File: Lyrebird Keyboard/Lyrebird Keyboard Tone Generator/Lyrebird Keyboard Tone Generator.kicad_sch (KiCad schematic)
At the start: 111 parts, among them IC1 LM358DT, IC10 LM358DT, IC11 LM358DT, IC12 LM358DT, IC13 HEF4069UBT,653, IC14 HEF4069UBT,653, IC2 LM358DT, IC3 LM358DT, IC4 LM358DT, IC5 LM358DT, IC6 LM358DT, IC7 LM358DT, IC8 LM358DT, IC9 LM358DT, J1 Edge Connector, J10 C# 4434 Hz, J11 G# 6642 Hz, J12 D 4697 Hz, J13 F# 5923 Hz, J2 A 3520 Hz, J3 D# 4976 Hz, J4 A# 3726 Hz, J5 E 5274 Hz, J6 B 3949 Hz, J7 F 5590 Hz, J8 C 4188 Hz, J9 G 6275 Hz

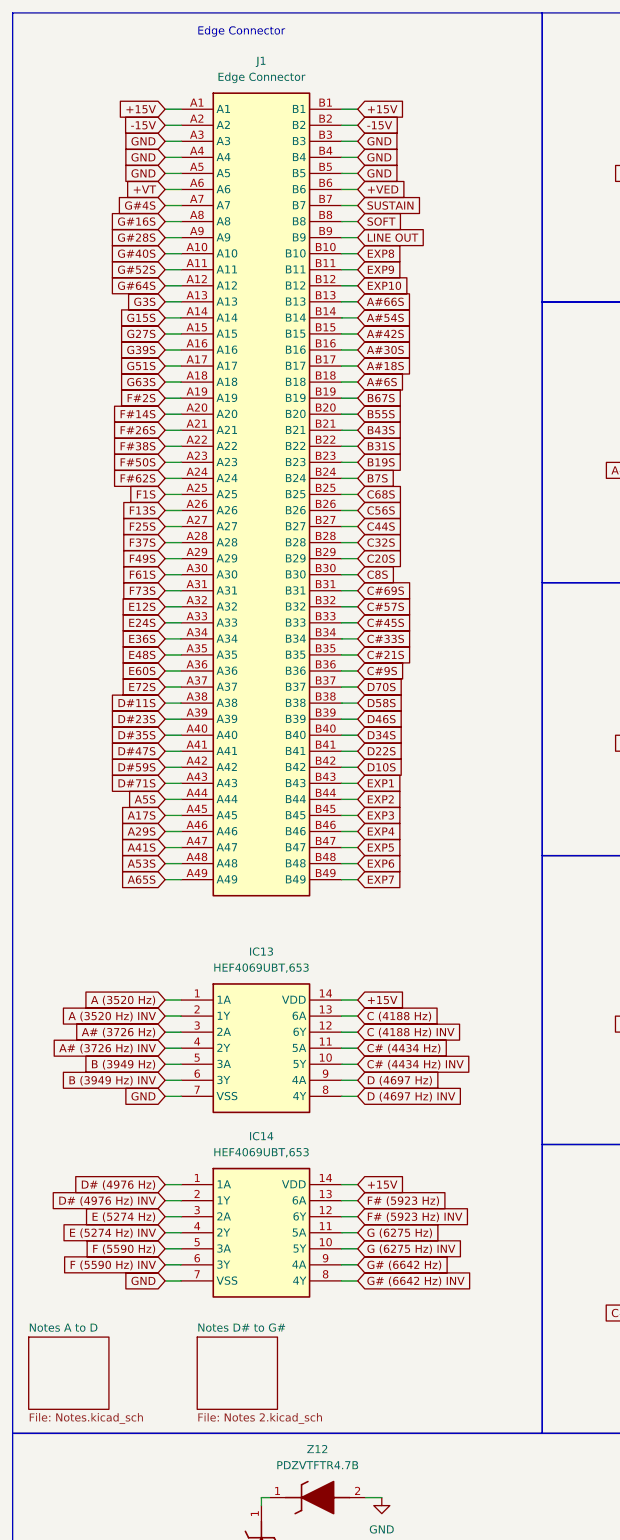
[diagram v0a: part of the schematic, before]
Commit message: Major Design Changes
Completed Tone Generator Board, board now only provides base notes, individual notes will be generated on the wave shaping boards.

Made major changes to pci slot config, and have increased grounding of the slots.

May need decoupling capacitors on tone generator board, but tight for room
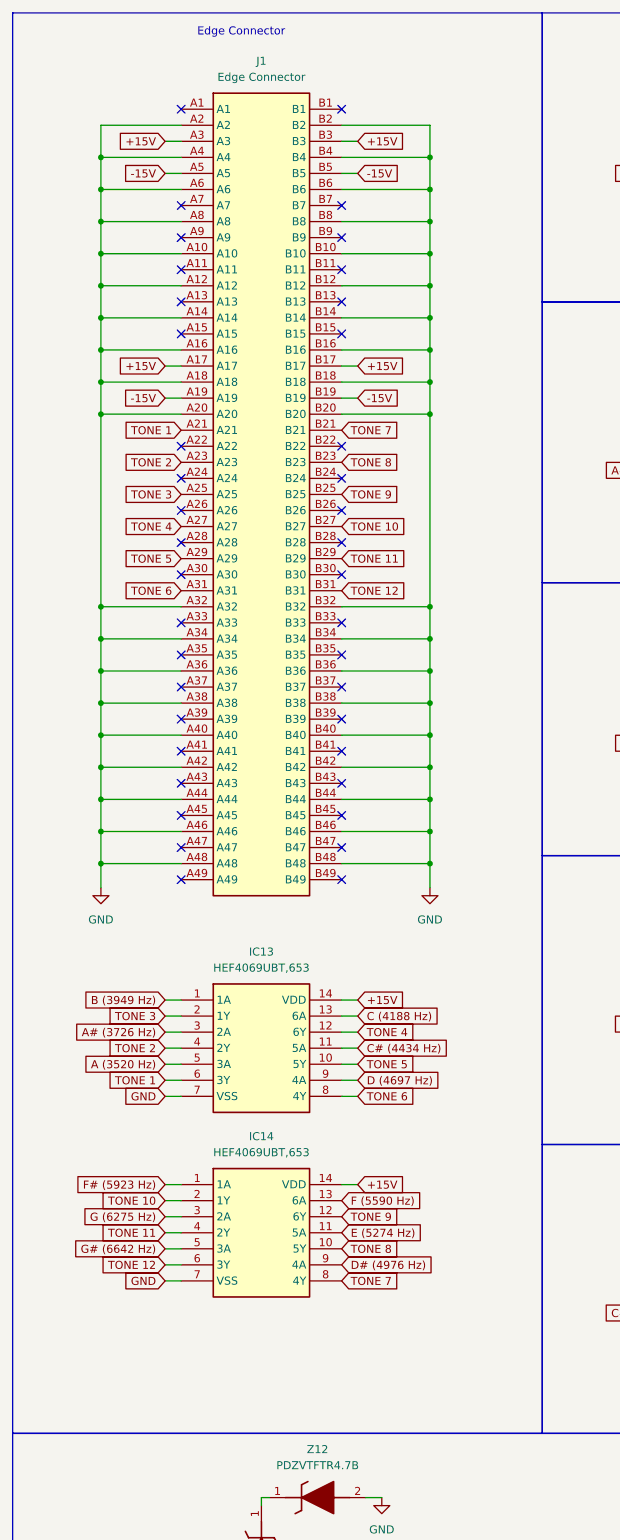
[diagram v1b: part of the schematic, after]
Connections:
- net +VED is gone; now on net GND: J1.B6
- net +VT is gone; now on net GND: J1.A6
- net A#18S is gone; now on net +15V: J1.B17
- net A#30S is gone; now on net GND: J1.B16
- net A#54S is gone; now on net GND: J1.B14
- net A#6S is gone; now on net GND: J1.B18
- net A29S is gone; now on net GND: J1.A46
- net A53S is gone; now on net GND: J1.A48
- net A5S is gone; now on net GND: J1.A44
- net B55S is gone; now on net GND: J1.B20
- net B67S is gone; now on net -15V: J1.B19
- net C#33S is gone; now on net GND: J1.B34
- net C#57S is gone; now on net GND: J1.B32
- net C#9S is gone; now on net GND: J1.B36
- net D# (4976 Hz) INV is gone; now on net TONE 10: IC14.2 (1Y)
- net D#11S is gone; now on net GND: J1.A38
- net D#35S is gone; now on net GND: J1.A40
- net D#59S is gone; now on net GND: J1.A42
- net D10S is gone; now on net GND: J1.B42
- net D34S is gone; now on net GND: J1.B40
- net D58S is gone; now on net GND: J1.B38
- net E (5274 Hz) INV is gone; now on net TONE 11: IC14.4 (2Y)
- net E12S is gone; now on net GND: J1.A32
- net E36S is gone; now on net GND: J1.A34
- net E60S is gone; now on net GND: J1.A36
- net EXP10 is gone; now on net GND: J1.B12
- net EXP2 is gone; now on net GND: J1.B44
- net EXP4 is gone; now on net GND: J1.B46
- net EXP6 is gone; now on net GND: J1.B48
- net EXP8 is gone; now on net GND: J1.B10
- net F (5590 Hz) INV is gone; now on net TONE 12: IC14.6 (3Y)
- net F# (5923 Hz) INV is gone; now on net TONE 9: IC14.12 (6Y)
- net F#14S is gone; now on net GND: J1.A20
- net F#26S is gone; now on net TONE 1: J1.A21
- net F#2S is gone; now on net -15V: J1.A19
- net F#50S is gone; now on net TONE 2: J1.A23
- net F1S is gone; now on net TONE 3: J1.A25
- net F25S is gone; now on net TONE 4: J1.A27
- net F49S is gone; now on net TONE 5: J1.A29
- net F73S is gone; now on net TONE 6: J1.A31
- net G (6275 Hz) INV is gone; now on net TONE 8: IC14.10 (5Y)
- net G# (6642 Hz) INV is gone; now on net TONE 7: IC14.8 (4Y)
- net G#16S is gone; now on net GND: J1.A8
- net G#40S is gone; now on net GND: J1.A10
- net G#64S is gone; now on net GND: J1.A12
- net G15S is gone; now on net GND: J1.A14
- net G39S is gone; now on net GND: J1.A16
- net G51S is gone; now on net +15V: J1.A17
- net G63S is gone; now on net GND: J1.A18
- net SOFT is gone; now on net GND: J1.B8
- net +15V: now also J1.A3, J1.B3; no longer J1.A1, J1.B1
- net -15V: now also J1.A5, J1.B5; no longer J1.A2, J1.B2
- net A (3520 Hz): now also IC13.5 (3A); no longer IC13.1 (1A)
- net B (3949 Hz): now also IC13.1 (1A); no longer IC13.5 (3A)
- net D# (4976 Hz): now also IC14.9 (4A); no longer IC14.1 (1A)
- net E (5274 Hz): now also IC14.11 (5A); no longer IC14.3 (2A)
- net F (5590 Hz): now also IC14.13 (6A); no longer IC14.5 (3A)
- net F# (5923 Hz): now also IC14.1 (1A); no longer IC14.13 (6A)
- net G (6275 Hz): now also IC14.3 (2A); no longer IC14.11 (5A)
- net G# (6642 Hz): now also IC14.5 (3A); no longer IC14.9 (4A)
- net GND: now also J1.A2, J1.B2; no longer J1.A3, J1.A5, J1.B3, J1.B5
- net A (3520 Hz) INV renamed TONE 3
- net A# (3726 Hz) INV renamed TONE 2
- net A#42S: no longer names the net of J1.B15
- net A#66S: no longer names the net of J1.B13
- net A17S: no longer names the net of J1.A45
- net A41S: no longer names the net of J1.A47
- net A65S: no longer names the net of J1.A49
- net B (3949 Hz) INV renamed TONE 1
- net B19S renamed TONE 8
- net B31S: no longer names the net of J1.B22
- net B43S renamed TONE 7
- net B7S: no longer names the net of J1.B24
- net C (4188 Hz) INV renamed TONE 4
- net C# (4434 Hz) INV renamed TONE 5
- net C#21S: no longer names the net of J1.B35
- net C#45S: no longer names the net of J1.B33
- net C#69S renamed TONE 12
- net C20S renamed TONE 11
- net C32S: no longer names the net of J1.B28
- net C44S renamed TONE 10
- net C56S: no longer names the net of J1.B26
- net C68S renamed TONE 9
- net C8S: no longer names the net of J1.B30
- net D (4697 Hz) INV renamed TONE 6
- net D#23S: no longer names the net of J1.A39
- net D#47S: no longer names the net of J1.A41
- net D#71S: no longer names the net of J1.A43
- net D22S: no longer names the net of J1.B41
- net D46S: no longer names the net of J1.B39
- net D70S: no longer names the net of J1.B37
- net E24S: no longer names the net of J1.A33
- net E48S: no longer names the net of J1.A35
- net E72S: no longer names the net of J1.A37
- net EXP1: no longer names the net of J1.B43
- net EXP3: no longer names the net of J1.B45
- net EXP5: no longer names the net of J1.B47
- net EXP7: no longer names the net of J1.B49
- net EXP9: no longer names the net of J1.B11
- net F#38S: no longer names the net of J1.A22
- net F#62S: no longer names the net of J1.A24
- net F13S: no longer names the net of J1.A26
- net F37S: no longer names the net of J1.A28
- net F61S: no longer names the net of J1.A30
- net G#28S: no longer names the net of J1.A9
- net G#4S: no longer names the net of J1.A7
- net G#52S: no longer names the net of J1.A11
- net G27S: no longer names the net of J1.A15
- net G3S: no longer names the net of J1.A13
- net LINE OUT: no longer names the net of J1.B9
- net SUSTAIN: no longer names the net of J1.B7
- no-connect marks 12 -> 52
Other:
- removed sheet Notes A to D
- removed sheet Notes D# to G#

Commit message: Schematic Updates
Made updates to schematics, to use correct symbols, and minor PCB updates, further work on the piano card design
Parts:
- removed IC1, IC10, IC11, IC12, IC2, IC3, IC4, IC5, IC6, IC7, IC8, IC9: LM358DT, SamacSys_Parts:SOIC127P600X175-8N, symbol SamacSys_Parts:LM358DT
- removed IC13, IC14: HEF4069UBT,653, SOIC127P600X175-14N, symbol SamacSys_Parts:HEF4069UBT,653
- added U1, U10, U11, U12, U2, U3, U4, U5, U6, U7, U8, U9: LM358, SamacSys_Parts:SOIC127P600X175-8N, symbol Amplifier_Operational:LM358
- added U13, U14: 4069, SamacSys_Parts:SOIC127P600X175-14N, symbol 4xxx:4069
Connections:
- net +15V: now also U1.8 (V+), U10.8 (V+), U11.8 (V+), U12.8 (V+), U13.14 (VDD), U14.14 (VDD), U2.8 (V+), U3.8 (V+), U4.8 (V+), U5.8 (V+), U6.8 (V+), U7.8 (V+), U8.8 (V+), U9.8 (V+)
- net -15V: now also U1.4 (V-), U10.4 (V-), U11.4 (V-), U12.4 (V-), U2.4 (V-), U3.4 (V-), U4.4 (V-), U5.4 (V-), U6.4 (V-), U7.4 (V-), U8.4 (V-), U9.4 (V-)
- net A (3520 Hz): now also R2.2, R3.2, U13.5; no longer R1.2, R3.1
- net A# (3726 Hz): now also R6.2, R7.2, U13.3; no longer R5.2, R7.1
- net B (3949 Hz): now also R10.2, R11.2, U13.1; no longer R11.1, R9.2
- net C (4188 Hz): now also R14.2, R15.2, R16.3, U13.13; no longer R13.2, R15.1, R16.1 (CCW)
- net C# (4434 Hz): now also R18.2, R19.2, R20.3, U13.11; no longer R17.2, R19.1, R20.1 (CCW)
- net D (4697 Hz): now also R22.2, R23.2, R24.3, U13.9; no longer R21.2, R23.1, R24.1 (CCW)
- net D# (4976 Hz): now also R26.2, R37.2, R43.3, U14.9; no longer R25.2, R37.1, R43.1 (CCW)
- net E (5274 Hz): now also R28.2, R38.2, R44.3, U14.11; no longer R27.2, R38.1, R44.1 (CCW)
- net F (5590 Hz): now also R30.2, R39.2, R45.3, U14.13; no longer R29.2, R39.1, R45.1 (CCW)
- net F# (5923 Hz): now also R36.2, R42.2, R48.3, U14.1; no longer R35.2, R42.1, R48.1 (CCW)
- net G (6275 Hz): now also R32.2, R40.2, R46.3, U14.3; no longer R31.2, R40.1, R46.1 (CCW)
- net G# (6642 Hz): now also R34.2, R41.2, R47.3, U14.5; no longer R33.2, R41.1, R47.1 (CCW)
- net GND: now also U1.2 (-), U1.5 (+), U10.2 (-), U10.5 (+), U11.2 (-), U11.5 (+), U12.2 (-), U12.5 (+), U13.7 (VSS), U14.7 (VSS), U2.2 (-), U2.5 (+), U3.2 (-), U3.5 (+), U4.2 (-), U4.5 (+), U5.2 (-), U5.5 (+), U6.2 (-), U6.5 (+), U7.2 (-), U7.5 (+), U8.2 (-), U8.5 (+), U9.2 (-), U9.5 (+)
- net TONE 1: now also U13.6
- net TONE 10: now also U14.2
- net TONE 11: now also U14.4
- net TONE 12: now also U14.6
- net TONE 2: now also U13.4
- net TONE 3: now also U13.2
- net TONE 4: now also U13.12
- net TONE 5: now also U13.10
- net TONE 6: now also U13.8
- net TONE 7: now also U14.8
- net TONE 8: now also U14.10
- net TONE 9: now also U14.12
- net at C5.1, R20.2: now also U5.6 (-)
- net at R31.1: now also C10.2, U11.7; no longer R32.2
- net at C10.1, R46.2: now also U11.6 (-)
- net at C12.1, R48.2: now also U10.6 (-)
- net at C1.1, R4.2: now also U1.6 (-)
- net at R29.1: now also C9.2, U9.7; no longer R30.2
- net at C8.1, R44.2: now also U8.6 (-)
- net at C9.1, R45.2: now also U9.6 (-)
- net at C7.1, R43.2: now also U7.6 (-)
- net at R1.1: now also C1.2, U1.7; no longer R2.2
- net at R13.1: now also C4.2, U4.7; no longer R14.2
- net at C2.1, R8.2: now also U2.6 (-)
- net at C6.1, R24.2: now also U6.6 (-)
- net at C3.1, R12.2: now also U3.6 (-)
- net at R5.1: now also C2.2, U2.7; no longer R6.2
- net at C4.1, R16.2: now also U4.6 (-)
- net at R17.1: now also C5.2, U5.7; no longer R18.2
- net at R33.1: now also C11.2, U12.7; no longer R34.2
- net at C11.1, R47.2: now also U12.6 (-)
- net at R9.1: now also C3.2, U3.7; no longer R10.2
- net at R27.1: now also C8.2, U8.7; no longer R28.2
- net at R21.1: now also C6.2, U6.7; no longer R22.2
- net at R25.1: now also C7.2, U7.7; no longer R26.2
- net at R35.1: now also C12.2, U10.7; no longer R36.2
- net TRI WAVE OUT (A#): no longer names the net of R6.1
- net TRI WAVE OUT (A#): now also R5.2, U2.3 (+); no longer C2.2
- net TRI WAVE OUT (A): no longer names the net of R2.1
- net TRI WAVE OUT (A): now also R1.2, U1.3 (+); no longer C1.2
- net TRI WAVE OUT (B): no longer names the net of R10.1
- net TRI WAVE OUT (B): now also R9.2, U3.3 (+); no longer C3.2
- net TRI WAVE OUT (C#): no longer names the net of R18.1
- net TRI WAVE OUT (C#): now also R17.2, U5.3 (+); no longer C5.2
- net TRI WAVE OUT (C): no longer names the net of R14.1
- net TRI WAVE OUT (C): now also R13.2, U4.3 (+); no longer C4.2
- net TRI WAVE OUT (D#): no longer names the net of R26.1
- net TRI WAVE OUT (D#): now also R25.2, U7.3 (+); no longer C7.2
- net TRI WAVE OUT (D): no longer names the net of R22.1
- net TRI WAVE OUT (D): now also R21.2, U6.3 (+); no longer C6.2
- net TRI WAVE OUT (E): no longer names the net of R28.1
- net TRI WAVE OUT (E): now also R27.2, U8.3 (+); no longer C8.2
- net TRI WAVE OUT (F#): no longer names the net of R36.1
- net TRI WAVE OUT (F#): now also R35.2, U10.3 (+); no longer C12.2
- net TRI WAVE OUT (F): no longer names the net of R30.1
- net TRI WAVE OUT (F): now also R29.2, U9.3 (+); no longer C9.2
- net TRI WAVE OUT (G#): no longer names the net of R34.1
- net TRI WAVE OUT (G#): now also R33.2, U12.3 (+); no longer C11.2
- net TRI WAVE OUT (G): no longer names the net of R32.1
- net TRI WAVE OUT (G): now also R31.2, U11.3 (+); no longer C10.2
- new net: R38.1, U8.1
- new net: R3.1, U1.1
- new net: R37.1, U7.1
- new net: R15.1, U4.1
- new net: R11.1, U3.1
- new net: R39.1, U9.1
- new net: R7.1, U2.1
- new net: R23.1, U6.1
- new net: R41.1, U12.1
- new net: R40.1, U11.1
- new net: R19.1, U5.1
- new net: R42.1, U10.1
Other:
- moved on the sheet: C1, C10, C11, C12, C2, C3, C4, C5, C6, C7, C8, C9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
